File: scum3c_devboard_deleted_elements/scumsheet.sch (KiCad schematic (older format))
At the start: 15 parts, among them U8 scum3

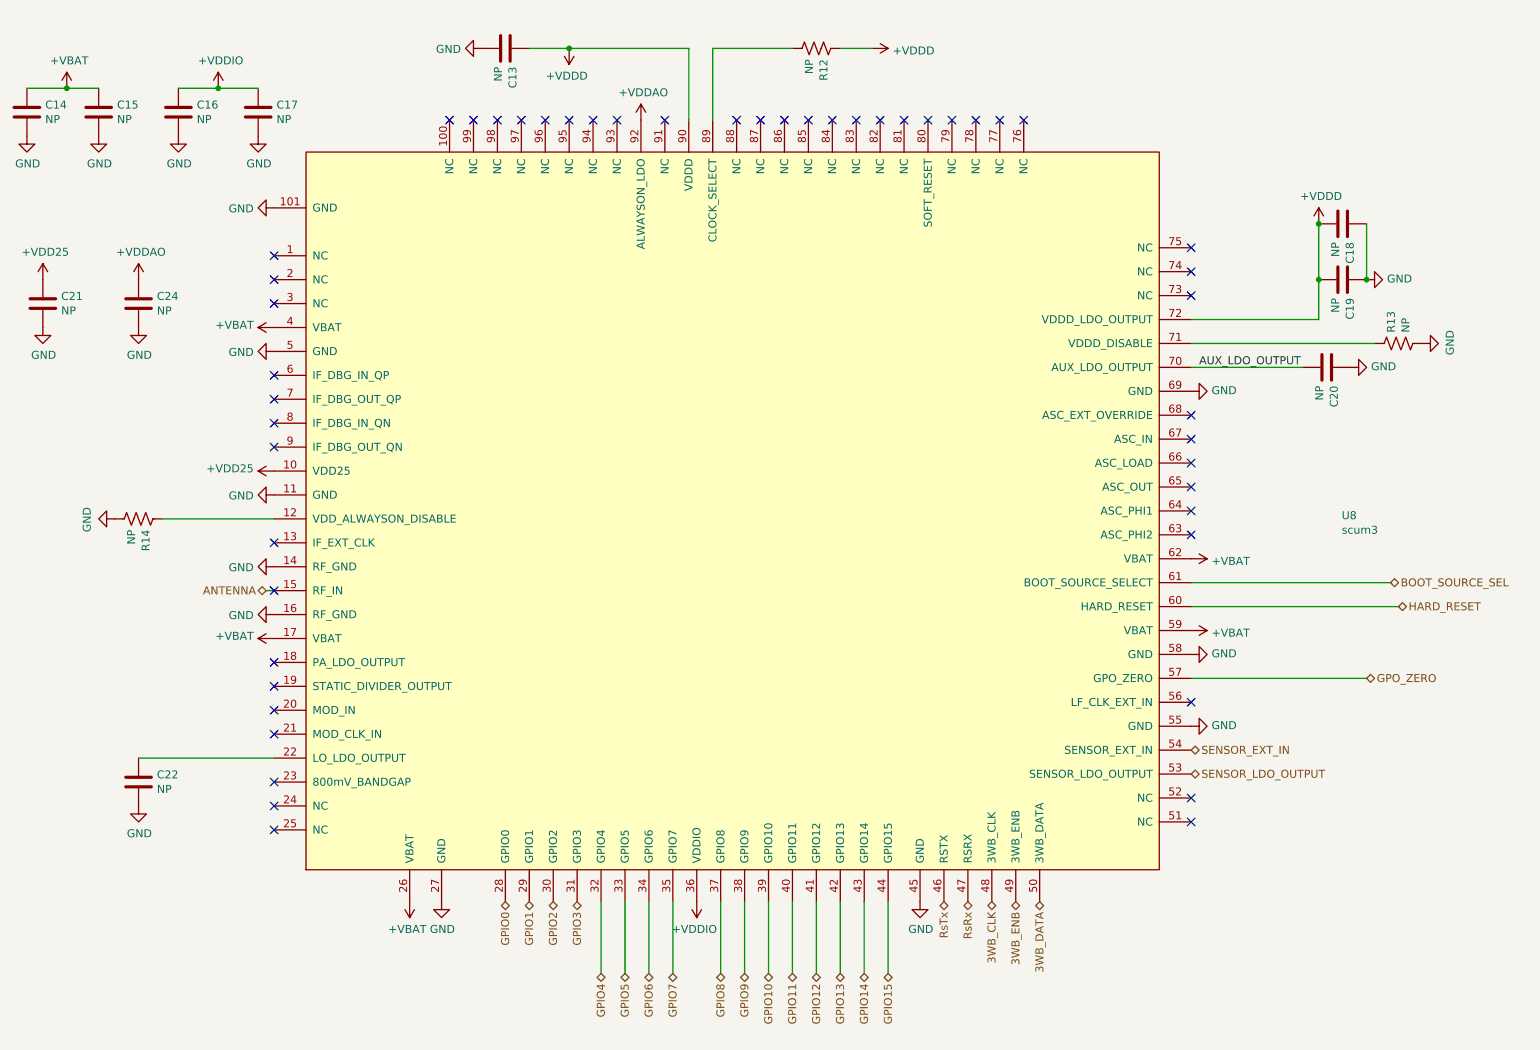
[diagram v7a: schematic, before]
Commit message: filled zones
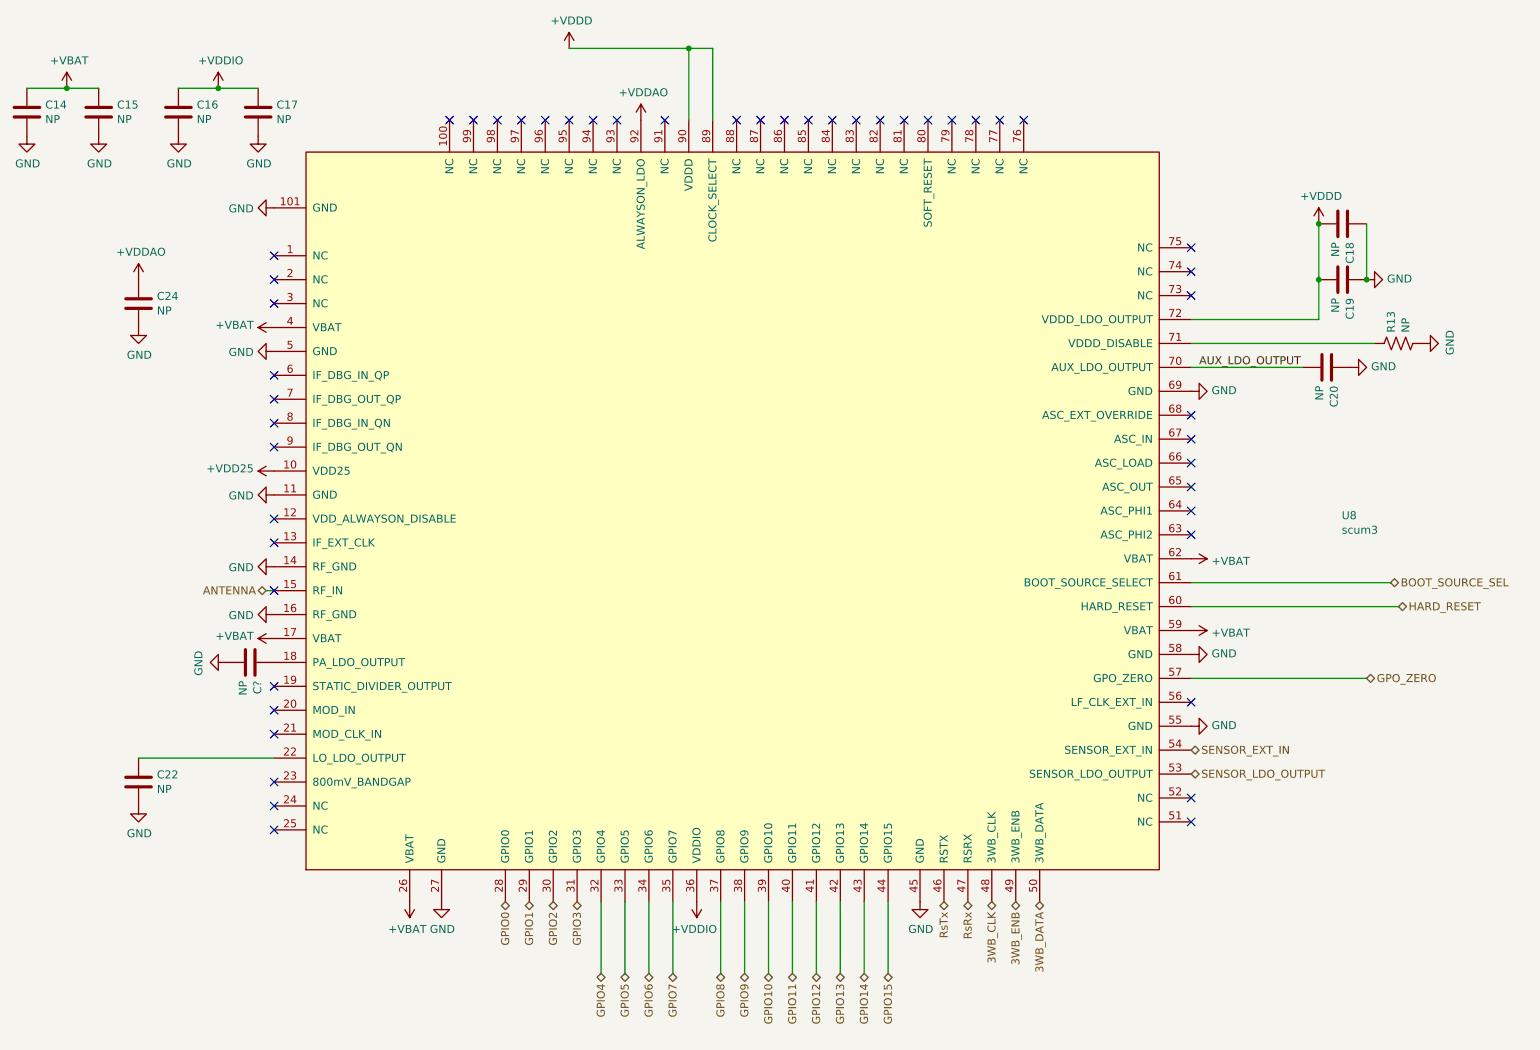
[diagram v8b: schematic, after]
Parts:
- removed C13, C21: NP, Capacitor_SMD:C_0402_1005Metric, symbol Device:C
- removed R12, R14: NP, Resistor_SMD:R_0402_1005Metric, symbol Device:R_US
- added C?: NP, Capacitor_SMD:C_0402_1005Metric, symbol Device:C
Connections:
- net +VDDD: now also U8.89 (CLOCK_SELECT)
- net GND: now also C?.2
- net at U8.18 (PA_LDO_OUTPUT): now also C?.1
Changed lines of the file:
@@
 NoConn ~ 2250 3200
 NoConn ~ 2250 3800
-NoConn ~ 2250 4550
 NoConn ~ 2250 4700
 NoConn ~ 2250 4850
@@
 $EndComp
 $Comp
-L Device:R_US R14
-U 1 1 5F419870
-P 1400 3650
-AR Path="/5F3B1D81/5F419870" Ref="R14"  Part="1"
-AR Path="/5F41418C/5F419870" Ref="R?"  Part="1"
-AR Path="/5F414989/5F419870" Ref="R?"  Part="1"
-F 0 "R14" H 1468 3696 50  0000 L CNN
-F 1 "NP" H 1468 3605 50  0000 L CNN
-F 2 "Resistor_SMD:R_0402_1005Metric" V 1440 3640 50  0001 C CNN
-F 3 "~" H 1400 3650 50  0001 C CNN
-	1    1400 3650
-	0    1    1    0
-$EndComp
-$Comp
 L power:GND #PWR0201
 U 1 1 5F419E58
@@
 $EndComp
 $Comp
-L power:GND #PWR0202
-U 1 1 5F41A5FE
-P 1250 3650
-AR Path="/5F3B1D81/5F41A5FE" Ref="#PWR0202"  Part="1"
-AR Path="/5F41418C/5F41A5FE" Ref="#PWR?"  Part="1"
-AR Path="/5F414989/5F41A5FE" Ref="#PWR?"  Part="1"
-F 0 "#PWR0202" H 1250 3400 50  0001 C CNN
-F 1 "GND" H 1255 3477 50  0000 C CNN
-F 2 "" H 1250 3650 50  0001 C CNN
-F 3 "" H 1250 3650 50  0001 C CNN
-	1    1250 3650
-	0    1    1    0
-$EndComp
-$Comp
 L draft1library:+VDDAO #PWR0205
 U 1 1 5F3A3049
@@
 $EndComp
 $Comp
-L power:GND #PWR0206
-U 1 1 5F3A4A87
-P 3550 700
-AR Path="/5F3B1D81/5F3A4A87" Ref="#PWR0206"  Part="1"
-AR Path="/5F41418C/5F3A4A87" Ref="#PWR?"  Part="1"
-AR Path="/5F414989/5F3A4A87" Ref="#PWR?"  Part="1"
-F 0 "#PWR0206" H 3550 450 50  0001 C CNN
-F 1 "GND" V 3555 572 50  0000 R CNN
-F 2 "" H 3550 700 50  0001 C CNN
-F 3 "" H 3550 700 50  0001 C CNN
-	1    3550 700
-	0    1    1    0
-$EndComp
-$Comp
-L Device:C C13
-U 1 1 5F3A5D08
-P 3700 700
-AR Path="/5F3B1D81/5F3A5D08" Ref="C13"  Part="1"
-AR Path="/5F41418C/5F3A5D08" Ref="C?"  Part="1"
-AR Path="/5F414989/5F3A5D08" Ref="C?"  Part="1"
-F 0 "C13" H 3815 746 50  0000 L CNN
-F 1 "NP" H 3815 655 50  0000 L CNN
-F 2 "Capacitor_SMD:C_0402_1005Metric" H 3738 550 50  0001 C CNN
-F 3 "~" H 3700 700 50  0001 C CNN
-	1    3700 700
-	0    1    1    0
-$EndComp
-$Comp
 L draft1library:+VDDD #PWR0207
 U 1 1 5F3A7150
@@
 F 3 "" H 4100 700 50  0001 C CNN
 	1    4100 700
-	-1   0    0    1
+	1    0    0    -1
 $EndComp
 Wire Wire Line
@@
 Wire Wire Line
 	4850 700  4100 700
-Wire Wire Line
-	3850 700  4100 700
-Connection ~ 4100 700
-$Comp
-L draft1library:+VDDD #PWR0208
-U 1 1 5F3A8DE4
-P 6000 700
-AR Path="/5F3B1D81/5F3A8DE4" Ref="#PWR0208"  Part="1"
-AR Path="/5F41418C/5F3A8DE4" Ref="#PWR?"  Part="1"
-AR Path="/5F414989/5F3A8DE4" Ref="#PWR?"  Part="1"
-F 0 "#PWR0208" H 6000 550 50  0001 C CNN
-F 1 "+VDDD" V 6015 828 50  0000 L CNN
-F 2 "" H 6000 700 50  0001 C CNN
-F 3 "" H 6000 700 50  0001 C CNN
-	1    6000 700
-	0    1    1    0
-$EndComp
-$Comp
-L Device:R_US R12
-U 1 1 5F3A9D0E
-P 5650 700
-AR Path="/5F3B1D81/5F3A9D0E" Ref="R12"  Part="1"
-AR Path="/5F41418C/5F3A9D0E" Ref="R?"  Part="1"
-AR Path="/5F414989/5F3A9D0E" Ref="R?"  Part="1"
-F 0 "R12" H 5718 746 50  0000 L CNN
-F 1 "NP" H 5718 655 50  0000 L CNN
-F 2 "Resistor_SMD:R_0402_1005Metric" V 5690 690 50  0001 C CNN
-F 3 "~" H 5650 700 50  0001 C CNN
-	1    5650 700
-	0    1    1    0
-$EndComp
-Wire Wire Line
-	6000 700  5800 700
-Wire Wire Line
-	5500 700  5000 700
 Wire Wire Line
 	5000 700  5000 1150
@@
 	5350 6500 5350 6050
 $Comp
-L power:GND #PWR0190
-U 1 1 5F3FB8E1
-P 800 2450
-AR Path="/5F3B1D81/5F3FB8E1" Ref="#PWR0190"  Part="1"
-AR Path="/5F41418C/5F3FB8E1" Ref="#PWR?"  Part="1"
-AR Path="/5F414989/5F3FB8E1" Ref="#PWR?"  Part="1"
-F 0 "#PWR0190" H 800 2200 50  0001 C CNN
-F 1 "GND" H 805 2277 50  0000 C CNN
-F 2 "" H 800 2450 50  0001 C CNN
-F 3 "" H 800 2450 50  0001 C CNN
-	1    800  2450
-	1    0    0    -1
-$EndComp
-$Comp
-L draft1library:+VDD25 #PWR0188
-U 1 1 5F3F91ED
-P 800 2150
-AR Path="/5F3B1D81/5F3F91ED" Ref="#PWR0188"  Part="1"
-AR Path="/5F41418C/5F3F91ED" Ref="#PWR?"  Part="1"
-AR Path="/5F414989/5F3F91ED" Ref="#PWR?"  Part="1"
-F 0 "#PWR0188" H 800 2000 50  0001 C CNN
-F 1 "+VDD25" H 815 2323 50  0000 C CNN
-F 2 "" H 800 2150 50  0001 C CNN
-F 3 "" H 800 2150 50  0001 C CNN
-	1    800  2150
-	1    0    0    -1
-$EndComp
-$Comp
-L Device:C C21
-U 1 1 5F3FABA5
-P 800 2300
-AR Path="/5F3B1D81/5F3FABA5" Ref="C21"  Part="1"
-AR Path="/5F41418C/5F3FABA5" Ref="C?"  Part="1"
-AR Path="/5F414989/5F3FABA5" Ref="C?"  Part="1"
-F 0 "C21" H 915 2346 50  0000 L CNN
-F 1 "NP" H 915 2255 50  0000 L CNN
-F 2 "Capacitor_SMD:C_0402_1005Metric" H 838 2150 50  0001 C CNN
-F 3 "~" H 800 2300 50  0001 C CNN
-	1    800  2300
-	1    0    0    -1
-$EndComp
-$Comp
 L draft1library:+VDD25 #PWR0192
 U 1 1 5F3FC7C2
@@
 Wire Wire Line
 	2250 5150 1400 5150
-Wire Wire Line
-	2250 3650 1550 3650
 NoConn ~ 2250 4100
+Text HLabel 2200 4100 0    50   BiDi ~ 0
+ANTENNA
+Wire Wire Line
+	2200 4100 2250 4100
+Wire Wire Line
+	8000 4200 9300 4200
+Text HLabel 9300 4200 2    50   BiDi ~ 0
+HARD_RESET
+Text HLabel 5500 6500 3    50   BiDi ~ 0
+GPIO11
+Wire Wire Line
+	5500 6050 5500 6500
+Wire Wire Line
+	8000 4650 9100 4650
+Text HLabel 9100 4650 2    50   BiDi ~ 0
+GPO_ZERO
 $Comp
 L draft1library:scum3 U8
@@
 	1    0    0    -1
 $EndComp
-Text HLabel 2200 4100 0    50   BiDi ~ 0
-ANTENNA
-Wire Wire Line
-	2200 4100 2250 4100
-Wire Wire Line
-	8000 4200 9300 4200
-Text HLabel 9300 4200 2    50   BiDi ~ 0
-HARD_RESET
-Text HLabel 5500 6500 3    50   BiDi ~ 0
-GPIO11
-Wire Wire Line
-	5500 6050 5500 6500
-Wire Wire Line
-	8000 4650 9100 4650
-Text HLabel 9100 4650 2    50   BiDi ~ 0
-GPO_ZERO
+NoConn ~ 2250 3650
+Wire Wire Line
+	5000 700  4850 700
+Connection ~ 4850 700
+$Comp
+L Device:C C?
+U 1 1 6085A679
+P 2100 4550
+AR Path="/5F3B1D81/6085A679" Ref="C?"  Part="1"
+AR Path="/5F41418C/6085A679" Ref="C?"  Part="1"
+AR Path="/5F414989/6085A679" Ref="C?"  Part="1"
+F 0 "C?" H 2215 4596 50  0000 L CNN
+F 1 "NP" H 2215 4505 50  0000 L CNN
+F 2 "Capacitor_SMD:C_0402_1005Metric" H 2138 4400 50  0001 C CNN
+F 3 "~" H 2100 4550 50  0001 C CNN
+	1    2100 4550
+	0    1    1    0
+$EndComp
+$Comp
+L power:GND #PWR?
+U 1 1 6085A67F
+P 1950 4550
+AR Path="/5F3B1D81/6085A67F" Ref="#PWR?"  Part="1"
+AR Path="/5F41418C/6085A67F" Ref="#PWR?"  Part="1"
+AR Path="/5F414989/6085A67F" Ref="#PWR?"  Part="1"
+F 0 "#PWR?" H 1950 4300 50  0001 C CNN
+F 1 "GND" H 1955 4377 50  0000 C CNN
+F 2 "" H 1950 4550 50  0001 C CNN
+F 3 "" H 1950 4550 50  0001 C CNN
+	1    1950 4550
+	0    1    1    0
+$EndComp
 $EndSCHEMATC
